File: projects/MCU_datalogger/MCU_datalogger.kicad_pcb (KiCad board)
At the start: 2 copper layers, 50.8 x 35.5 mm, 31 parts, among them J1 Conn_01x04_Pin, J2 Conn_01x09_Pin, J3 Conn_01x04_Pin, J4 Conn_02x03_Odd_Even, U1 24LC1025, U2 DS1337S_, U3 24LC1025, U4 ATMEGA328P-AU, Y1 32.768KHz, Y2 16MHz

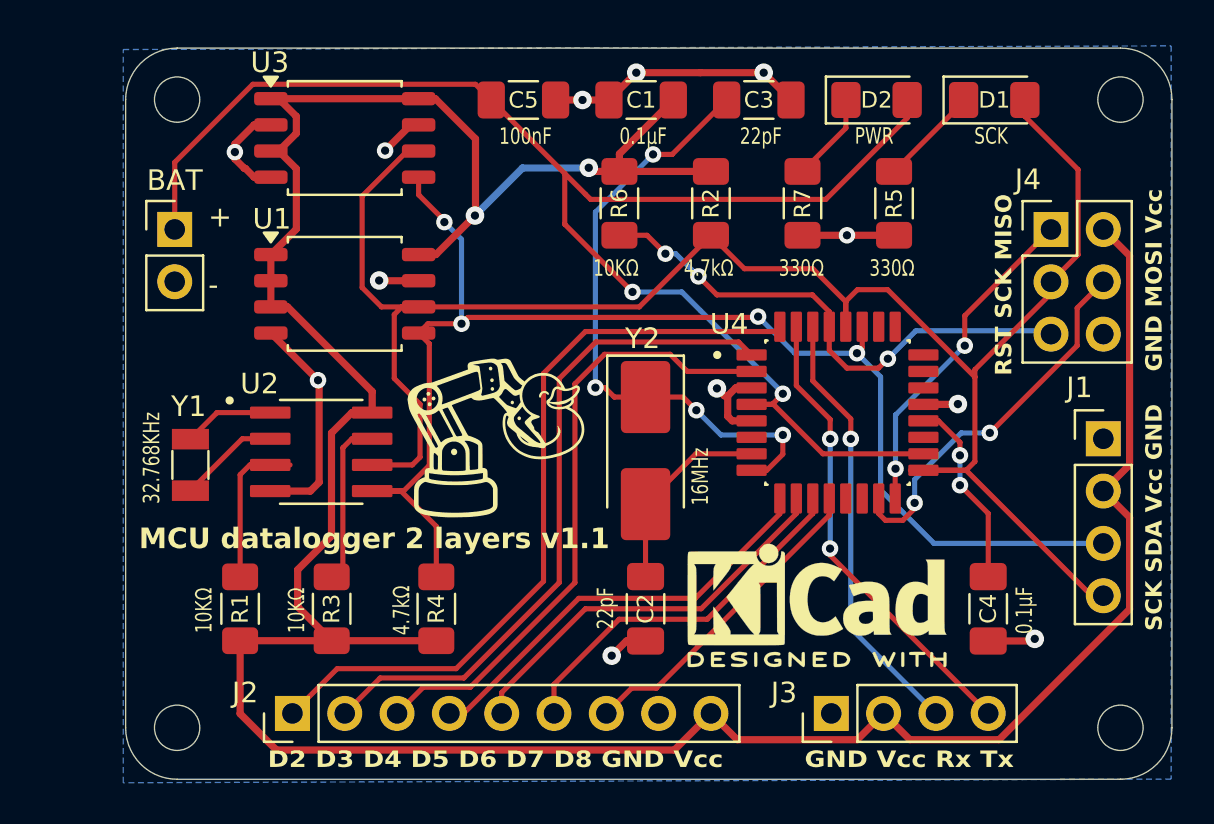
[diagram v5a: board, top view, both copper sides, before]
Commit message: MCU datalogger - v1.1 add Vcc fill zone, minor routing and silkscreen details
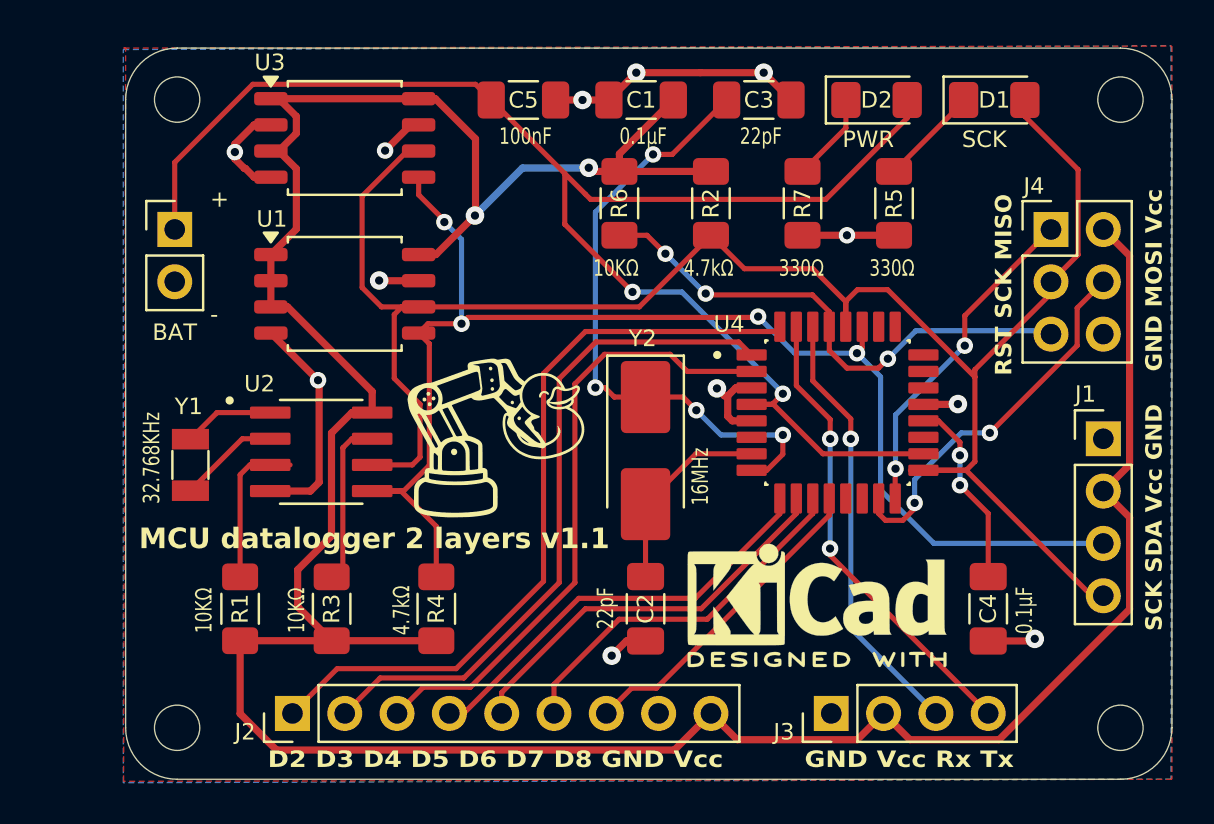
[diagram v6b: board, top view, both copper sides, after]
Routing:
- added copper zone on F.Cu, net /Vcc
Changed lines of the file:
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@@
 			(outputformat 1)
 			(mirror no)
-			(drillshape 1)
+			(drillshape 0)
 			(scaleselection 1)
-			(outputdirectory "")
+			(outputdirectory "gerbers")
 		)
 	)
@@
 			(effects
 				(font
-					(size 1 1)
-					(thickness 0.15)
+					(size 0.8 0.8)
+					(thickness 0.12)
 				)
 			)
@@
 			(effects
 				(font
-					(size 1 1)
-					(thickness 0.15)
+					(size 0.8 0.8)
+					(thickness 0.12)
 				)
 			)
@@
 			(effects
 				(font
-					(size 1 1)
-					(thickness 0.15)
+					(size 0.8 0.8)
+					(thickness 0.12)
 				)
 			)
@@
 			(effects
 				(font
-					(size 1 1)
-					(thickness 0.15)
+					(size 0.8 0.8)
+					(thickness 0.12)
 				)
 			)
@@
 		(tags "Through hole pin header THT 1x04 2.54mm single row")
 		(property "Reference" "J1"
-			(at -1.16 -2.485 0)
+			(at -0.868 -2.167905 0)
 			(layer "F.SilkS")
 			(effects
 				(font
-					(size 1 1)
-					(thickness 0.15)
+					(size 0.8 0.8)
+					(thickness 0.12)
 				)
 			)
@@
 		(tags "Through hole pin header THT 1x09 2.54mm single row")
 		(property "Reference" "J2"
-			(at 1.002905 -2.298 180)
+			(at -0.897095 -2.298 180)
 			(layer "F.SilkS")
 			(effects
 				(font
-					(size 1 1)
-					(thickness 0.15)
+					(size 0.8 0.8)
+					(thickness 0.12)
 				)
 			)
@@
 			(effects
 				(font
-					(size 1 1)
-					(thickness 0.15)
+					(size 0.8 0.8)
+					(thickness 0.12)
 				)
 			)
@@
 		(tags "Through hole pin header THT 1x02 2.54mm single row")
 		(property "Reference" "BAT"
-			(at 0 -2.38 0)
+			(at 0 4.997095 0)
 			(layer "F.SilkS")
 			(effects
 				(font
-					(size 1 1)
-					(thickness 0.15)
+					(size 0.8 0.8)
+					(thickness 0.18)
 				)
 			)
@@
 		(tags "Through hole pin header THT 1x04 2.54mm single row")
 		(property "Reference" "J3"
-			(at 1.002905 -2.298 180)
+			(at -0.897095 -2.298 180)
 			(layer "F.SilkS")
 			(effects
 				(font
-					(size 1 1)
-					(thickness 0.15)
+					(size 0.8 0.8)
+					(thickness 0.12)
 				)
 			)
@@
 		(tags "Through hole pin header THT 2x03 2.54mm double row")
 		(property "Reference" "J4"
-			(at -1.12 -2.425 0)
+			(at -0.828 -2.107905 0)
 			(layer "F.SilkS")
 			(effects
 				(font
-					(size 1 1)
-					(thickness 0.15)
+					(size 0.8 0.8)
+					(thickness 0.12)
 				)
 			)
@@
 			(effects
 				(font
-					(size 1 1)
-					(thickness 0.15)
+					(size 0.8 0.8)
+					(thickness 0.12)
 				)
 			)
@@
 	)
 	(gr_text "PWR"
-		(at 176.4 86.0365 0)
+		(at 175.8 86.2 0)
 		(layer "F.SilkS")
 		(effects
 			(font
-				(size 0.8 0.6)
-				(thickness 0.1)
+				(size 0.8 0.8)
+				(thickness 0.18)
 			)
 			(justify left bottom)
@@
 	)
 	(gr_text "-"
-		(at 145.008 93.382905 0)
+		(at 145.1 94.7 0)
 		(layer "F.SilkS")
 		(effects
 			(font
-				(size 1 1)
-				(thickness 0.1)
+				(size 0.8 0.8)
+				(thickness 0.16)
 			)
 			(justify left bottom)
@@
 	)
 	(gr_text "SCK"
-		(at 182.2 86.0365 0)
+		(at 181.6 86.2 0)
 		(layer "F.SilkS")
 		(effects
 			(font
-				(size 0.8 0.6)
-				(thickness 0.1)
+				(size 0.8 0.8)
+				(thickness 0.18)
 			)
 			(justify left bottom)
@@
 	)
 	(gr_text "+"
-		(at 145.008 90.082905 0)
+		(at 145.1 89.1 0)
 		(layer "F.SilkS")
 		(effects
 			(font
-				(size 1 1)
-				(thickness 0.1)
+				(size 0.8 0.8)
+				(thickness 0.16)
 			)
 			(justify left bottom)
@@
 	)
 	(segment
-		(start 169.708 93.282905)
-		(end 174.346 93.282905)
+		(start 175.163 94.099905)
+		(end 175.163 94.827905)
 		(width 0.25)
 		(layer "F.Cu")
@@
 	)
 	(segment
-		(start 168.808 92.382905)
-		(end 169.708 93.282905)
+		(start 169.228905 93.282905)
+		(end 174.346 93.282905)
 		(width 0.25)
 		(layer "F.Cu")
@@
 	)
 	(segment
-		(start 175.163 94.099905)
-		(end 175.163 94.827905)
+		(start 175.163 94.827905)
+		(end 175.163 95.979905)
 		(width 0.25)
 		(layer "F.Cu")
@@
 	)
 	(segment
-		(start 175.163 94.827905)
-		(end 175.163 95.979905)
+		(start 174.346 93.282905)
+		(end 175.163 94.099905)
 		(width 0.25)
 		(layer "F.Cu")
@@
 	)
 	(segment
-		(start 177.552 96.838905)
-		(end 178.008 96.382905)
+		(start 169.164 93.218)
+		(end 169.228905 93.282905)
 		(width 0.25)
 		(layer "F.Cu")
@@
 	)
 	(segment
-		(start 175.163 95.979905)
-		(end 176.022 96.838905)
+		(start 177.552 96.838905)
+		(end 178.008 96.382905)
 		(width 0.25)
 		(layer "F.Cu")
@@
 	)
 	(segment
-		(start 174.346 93.282905)
-		(end 175.163 94.099905)
+		(start 175.163 95.979905)
+		(end 176.022 96.838905)
 		(width 0.25)
 		(layer "F.Cu")
@@
 	)
 	(via
-		(at 168.808 92.382905)
+		(at 169.164 93.218)
 		(size 0.8)
 		(drill 0.4)
@@
 	)
 	(segment
-		(start 185.928 95.187905)
-		(end 185.763014 95.022919)
+		(start 169.143095 93.218)
+		(end 169.164 93.218)
 		(width 0.25)
 		(layer "B.Cu")
@@
 	)
 	(segment
-		(start 167.708 91.282905)
-		(end 168.808 92.382905)
+		(start 185.928 95.187905)
+		(end 185.763014 95.022919)
 		(width 0.25)
 		(layer "B.Cu")
@@
 	(segment
 		(start 167.208 91.282905)
-		(end 167.708 91.282905)
+		(end 169.143095 93.218)
 		(width 0.25)
 		(layer "B.Cu")
@@
 	)
 	(zone
+		(net 3)
+		(net_name "/Vcc")
+		(layer "F.Cu")
+		(hatch edge 0.5)
+		(priority 1)
+		(connect_pads
+			(clearance 0.5)
+		)
+		(min_thickness 0.25)
+		(filled_areas_thickness no)
+		(fill yes
+			(thermal_gap 0.5)
+			(thermal_bridge_width 0.5)
+		)
+		(polygon
+			(pts
+				(xy 140.9 81.3) (xy 191.8 81.2) (xy 191.8 116.8) (xy 140.9 116.9) (xy 141 81.3)
+			)
+		)
+	)
+	(zone

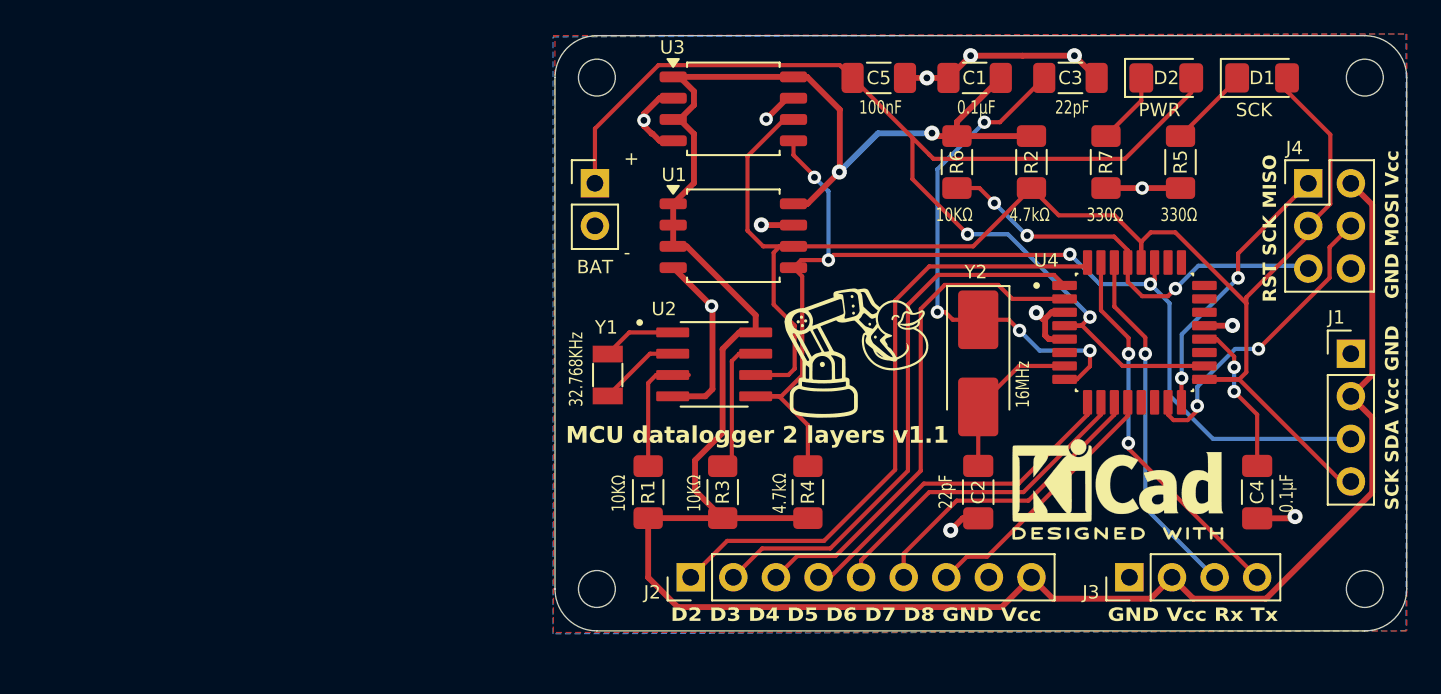
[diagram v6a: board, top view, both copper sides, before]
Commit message: MCU datalogger v1.2
- fix missing Vcc label in Battery + net
- fix the resulting violations of Vcc routing (wider tracks required)
- reorder pins of GPIO connector to make Pin 1 is GND
- Add silkscreen labels to connectors I2C ICSP Serial and GPIO
- other minor adjustments to component placements and silkscreen
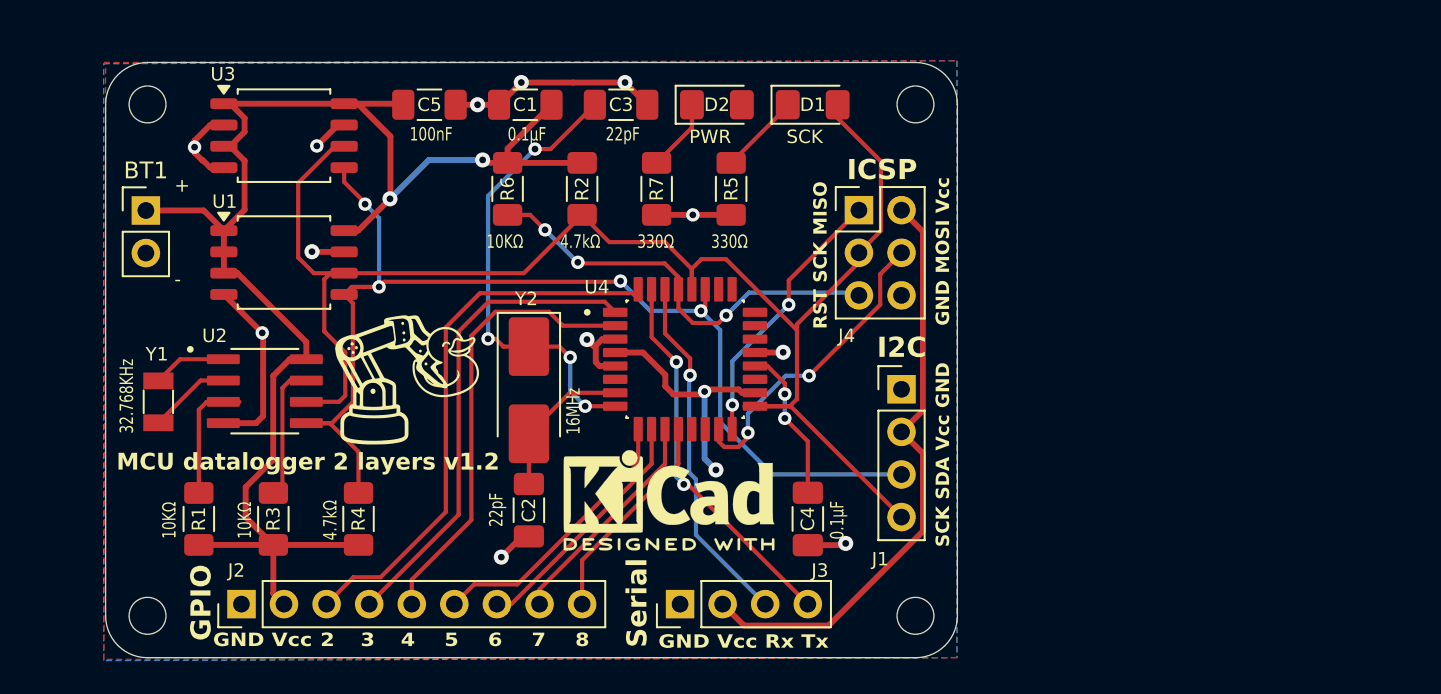
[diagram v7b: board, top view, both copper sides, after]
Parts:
- removed BAT: Battery, Connector_PinHeader_2.54mm:PinHeader_1x02_P2.54mm_Vertical
- added BT1: Battery, Connector_PinHeader_2.54mm:PinHeader_1x02_P2.54mm_Vertical, F.Cu at (116.6, 91.7)
- moved J1 26.9 mm to (161.7, 102.4)
- moved C1 26.8 mm to (139.2, 85.4)
- moved C3 26.8 mm to (144.9, 85.4)
- moved C5 26.8 mm to (133.5, 85.4)
- moved D1 26.8 mm to (156.4, 85.4)
- moved D2 26.8 mm to (150.7, 85.4)
- moved G*** 26.8 mm to (132.1, 101.4)
- moved H2 26.8 mm to (162.5, 85.4)
- moved H4 26.8 mm to (162.5, 115.9)
- moved J2 26.8 mm to (122.3, 115.2)
- moved J4 26.8 mm to (159.1, 91.7)
- moved R2 26.8 mm to (142.6, 90.4)
- moved R4 26.8 mm to (129.3, 110.1)
- moved R6 26.8 mm to (138.2, 90.4)
- moved R7 26.8 mm to (147.1, 90.4)
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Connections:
- C5 pad 2: Net-(BT1-+) -> /Vcc
- D2 pad 2: Net-(BT1-+) -> /Vcc
- J2 pad 1: /D2 -> GND
- J2 pad 2: /D3 -> /Vcc
- J2 pad 3: /D4 -> /D2
- J2 pad 4: /D5 -> /D3
- J2 pad 5: /D6 -> /D4
- J2 pad 6: /D7 -> /D5
- J2 pad 7: /D8 -> /D6
- J2 pad 8: GND -> /D7
- J2 pad 9: /Vcc -> /D8
- U4 pad 18: Net-(BT1-+) -> /Vcc
- U4 pad 4: Net-(BT1-+) -> /Vcc
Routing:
- net Net-(BT1-+): track 72.8 -> 0.00 mm, vias 2 -> 0
- net /Vcc: track 150.9 -> 141.5 mm, vias 2 -> 4
- net /D6: track 19.7 -> 14.8 mm
- net /D7: track 18.1 -> 13.5 mm
- net /D2: track 37.4 -> 32.8 mm
- net /D5: track 20.8 -> 16.5 mm
- net /D3: track 33.3 -> 29.5 mm
- net /D4: track 30.4 -> 27.0 mm
- net /D8: track 15.6 -> 12.3 mm
- net Net-(U4-PB7): track 30.2 -> 27.8 mm
- net /SCK: track 91.0 -> 91.8 mm
- net Net-(U4-PB6): track 9.68 -> 9.16 mm
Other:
- board text added: "2"
- board text added: "3"
- board text added: "4"
- board text added: "5"
- board text added: "6"
- board text added: "7"
- board text added: "8"
- board text added: "GND Vcc"
- board text added: "GPIO"
- board text added: "I2C"
- board text added: "ICSP"
- board text added: "MCU datalogger 2 layers v1.2"
- board text added: "Serial"
- board text removed: "D2 D3 D4 D5 D6 D7 D8 GND Vcc"
- board text removed: "MCU datalogger 2 layers v1.1"

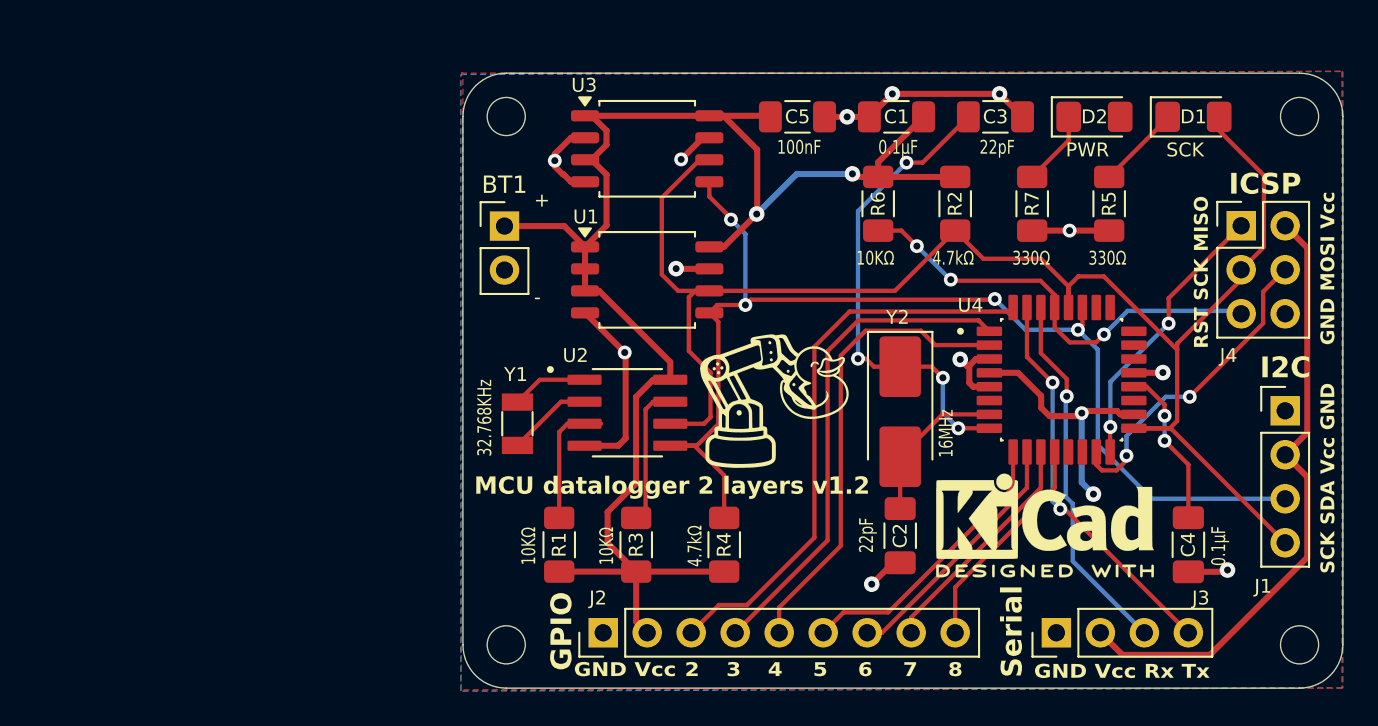
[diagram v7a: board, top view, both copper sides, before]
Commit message: MCU datalogger v1.2 - add logo and silkscreen at the back
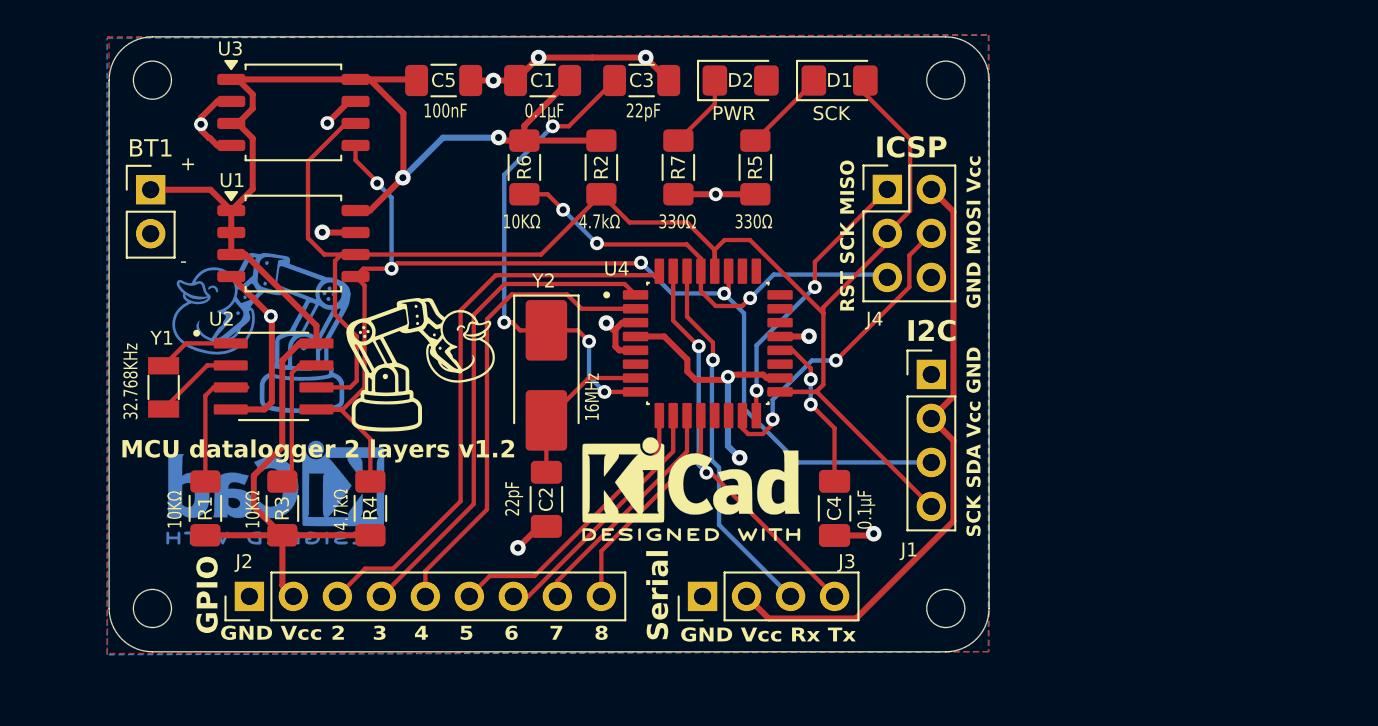
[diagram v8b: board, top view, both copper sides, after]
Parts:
- added G***: LOGO, MH_LOGO:robot_duckie_logo_12mm, B.Cu at (102.7, 97.4)
- added REF**: KiCad-Logo2_5mm_Copper, Symbol:KiCad-Logo2_5mm_Copper, B.Cu at (103.4, 107.1)
- moved C2 20.5 mm to (119.0, 107.5)
- moved REF** 20.5 mm to (127.4, 106.9)
- moved Y2 20.5 mm to (119.0, 100.3)
- moved H1 20.5 mm to (96.3, 83.3)
- moved H2 20.5 mm to (142.1, 83.3)
- moved H3 20.5 mm to (96.3, 113.8)
- moved H4 20.5 mm to (142.1, 113.8)
- moved BT1 20.5 mm to (96.2, 89.6)
- moved C3 20.5 mm to (124.5, 83.3)
- moved C4 20.5 mm to (135.7, 108.0)
- moved D1 20.5 mm to (135.9, 83.3)
- moved D2 20.5 mm to (130.2, 83.3)
- moved G*** 20.5 mm to (111.7, 99.3)
- moved J1 20.5 mm to (141.2, 100.3)
- moved J2 20.5 mm to (101.9, 113.1)
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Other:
- board text added: "0.2000 mm / 0.0000 mm"
- board text added: "0.3000 mm"
- board text added: "1.6000 mm"
- board text added: "2 Mbit EEPROM RTC I2C SPI GPIOs"
- board text added: "50.8000 mm x 35.5000 mm"
- board text added: "BOARD CHARACTERISTICS"
- board text added: "Board Thickness:"
- board text added: "Board overall dimensions:"
- board text added: "Castellated pads:"
- board text added: "Copper Finish:"
- board text added: "Copper Layer Count:"
- board text added: "Edge card connectors:"
- board text added: "Impedance Control:"
- board text added: "Min hole diameter:"
- board text added: "Min track/spacing:"
- board text added: "No"
- board text added: "None"
- board text added: "Plated Board Edge:"
